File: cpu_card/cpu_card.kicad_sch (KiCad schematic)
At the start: 23 parts, among them J101 PC/104 ISA, J102 SYSBUS, J103 80188, J104 256K ROM, U101 128K SRAM, Y1 16MHz

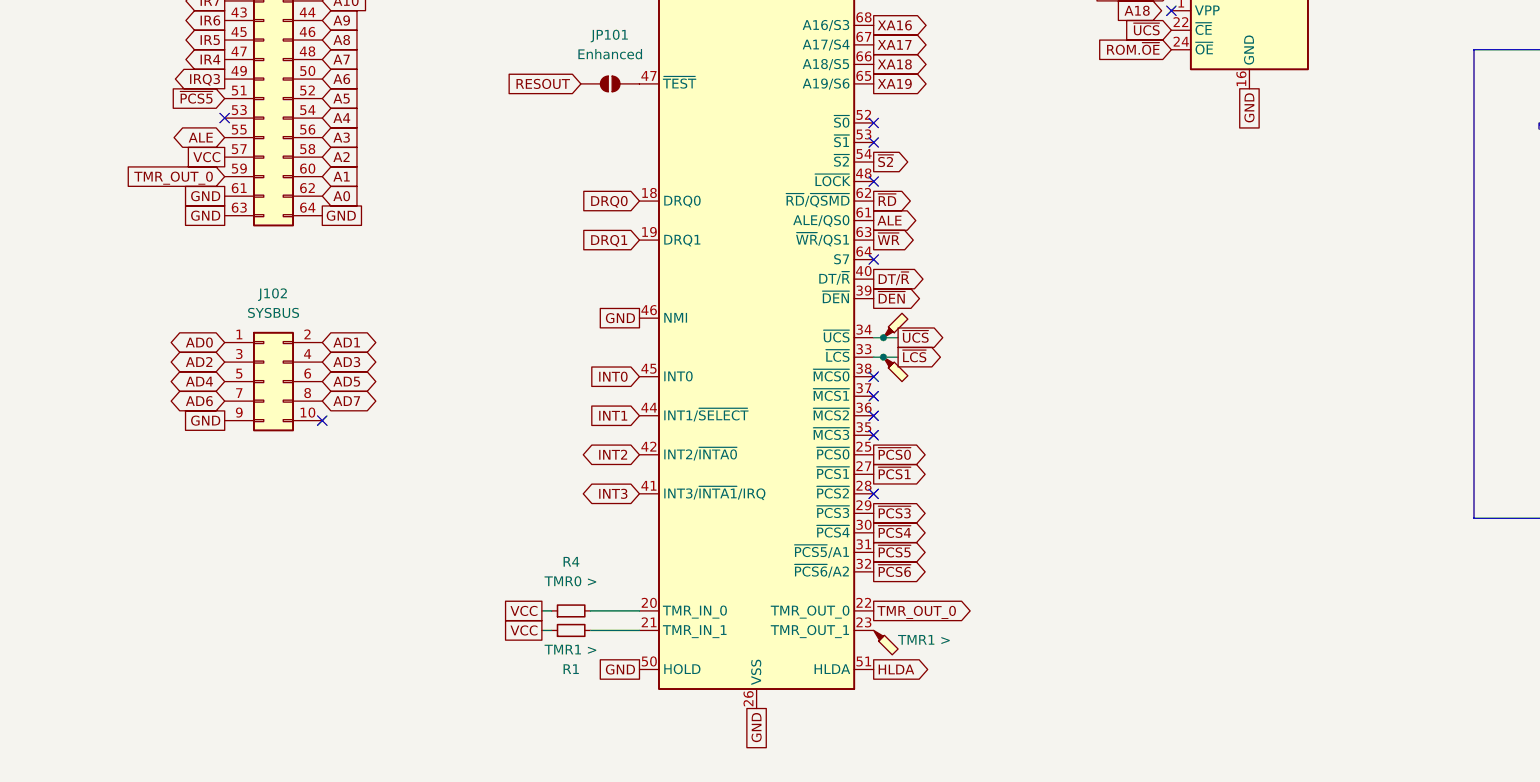
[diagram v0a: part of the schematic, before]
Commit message: bios library and overall cleanup
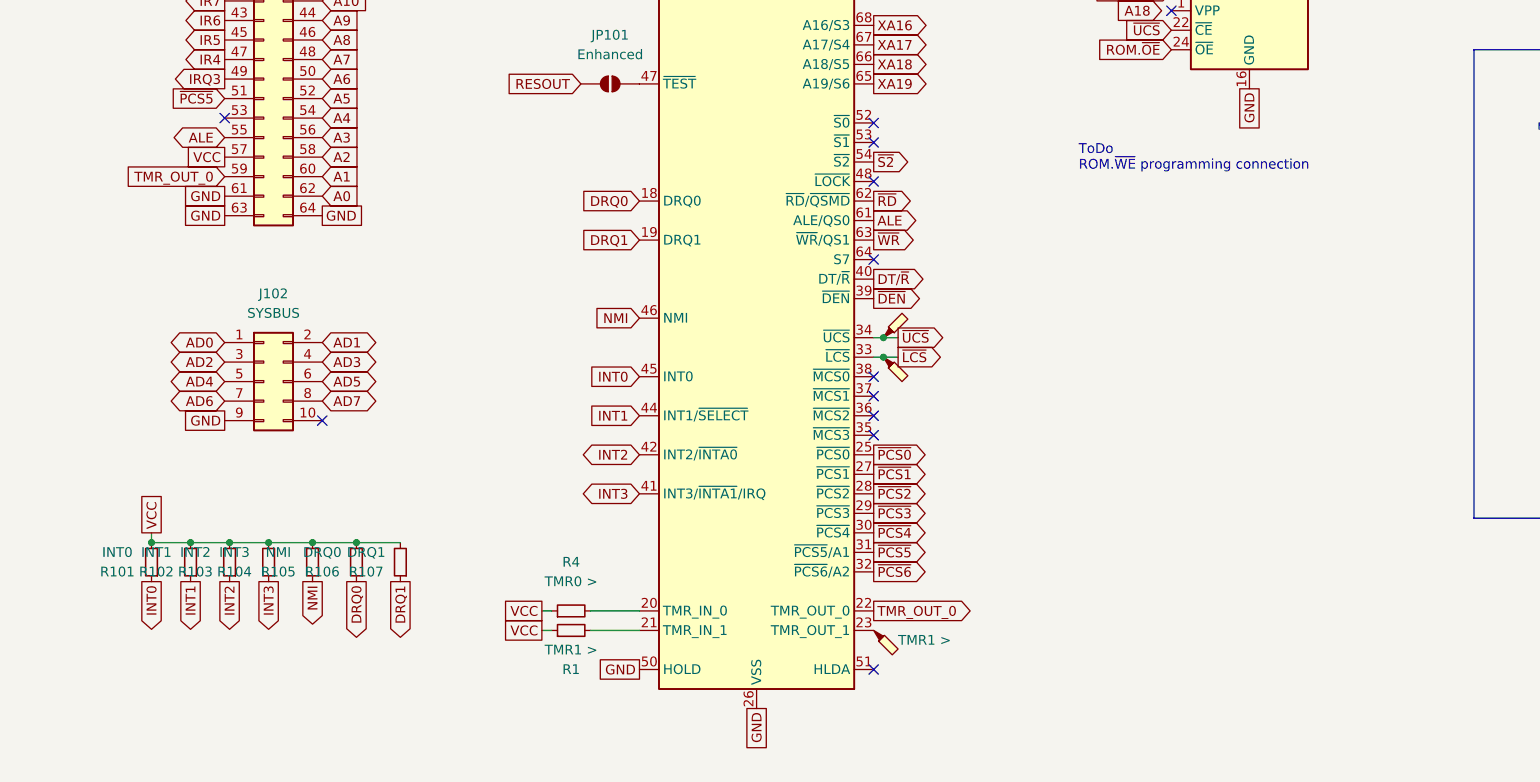
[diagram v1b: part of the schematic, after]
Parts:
- added R101: INT0, Resistor_SMD:R_1206_3216Metric_Pad1.30x1.75mm_HandSolder, symbol Device:R_Small
- added R102: INT1, Resistor_SMD:R_1206_3216Metric_Pad1.30x1.75mm_HandSolder, symbol Device:R_Small
- added R103: INT2, Resistor_SMD:R_1206_3216Metric_Pad1.30x1.75mm_HandSolder, symbol Device:R_Small
- added R104: INT3, Resistor_SMD:R_1206_3216Metric_Pad1.30x1.75mm_HandSolder, symbol Device:R_Small
- added R105: NMI, Resistor_SMD:R_1206_3216Metric_Pad1.30x1.75mm_HandSolder, symbol Device:R_Small
- added R106: DRQ0, Resistor_SMD:R_1206_3216Metric_Pad1.30x1.75mm_HandSolder, symbol Device:R_Small
- added R107: DRQ1, Resistor_SMD:R_1206_3216Metric_Pad1.30x1.75mm_HandSolder, symbol Device:R_Small
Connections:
- net +5VD: now also R101.2, R102.2, R103.2, R104.2, R105.2, R106.2, R107.2
- net DRQ0: now also R106.1
- net DRQ1: now also R107.1
- net GNDD: no longer J103.46 (NMI)
- net INT0: now also R101.1
- net INT1: now also R102.1
- net INT2: now also R103.1
- net INT3: now also R104.1
- net ~{PCS2}: now reaches J103.28 (~{PCS2})
- net HLDA: no longer names the net of J103.51 (HLDA)
- new net NMI: J103.46 (NMI), R105.1
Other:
- note added: "ToDo ROM.~{WE} programming connection"
